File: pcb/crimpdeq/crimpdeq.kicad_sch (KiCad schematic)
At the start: 49 parts, among them J2 USB4105-GF-A, Q1 SS8550, Q2 DMG3415U, SW1 SW_Push, SW2 SW_Push, U1 ESP32-C3-MINI-1, U2 MCP73831T-2ACI/OT, U3 HX711, U4 Rust_Board, U6 SY8088

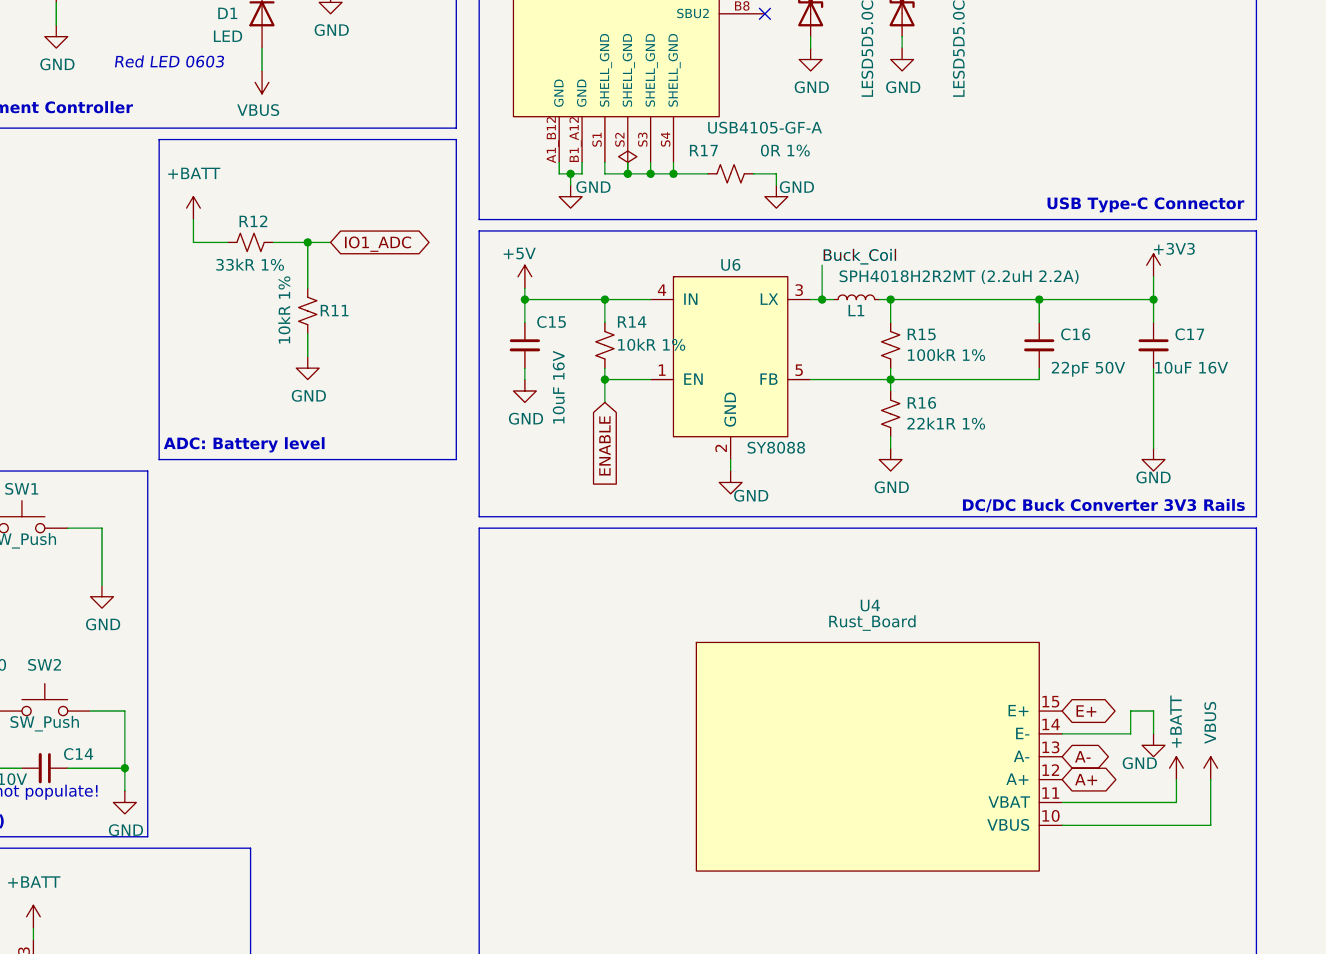
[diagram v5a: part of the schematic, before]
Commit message: fix: allow battery charging while powered off
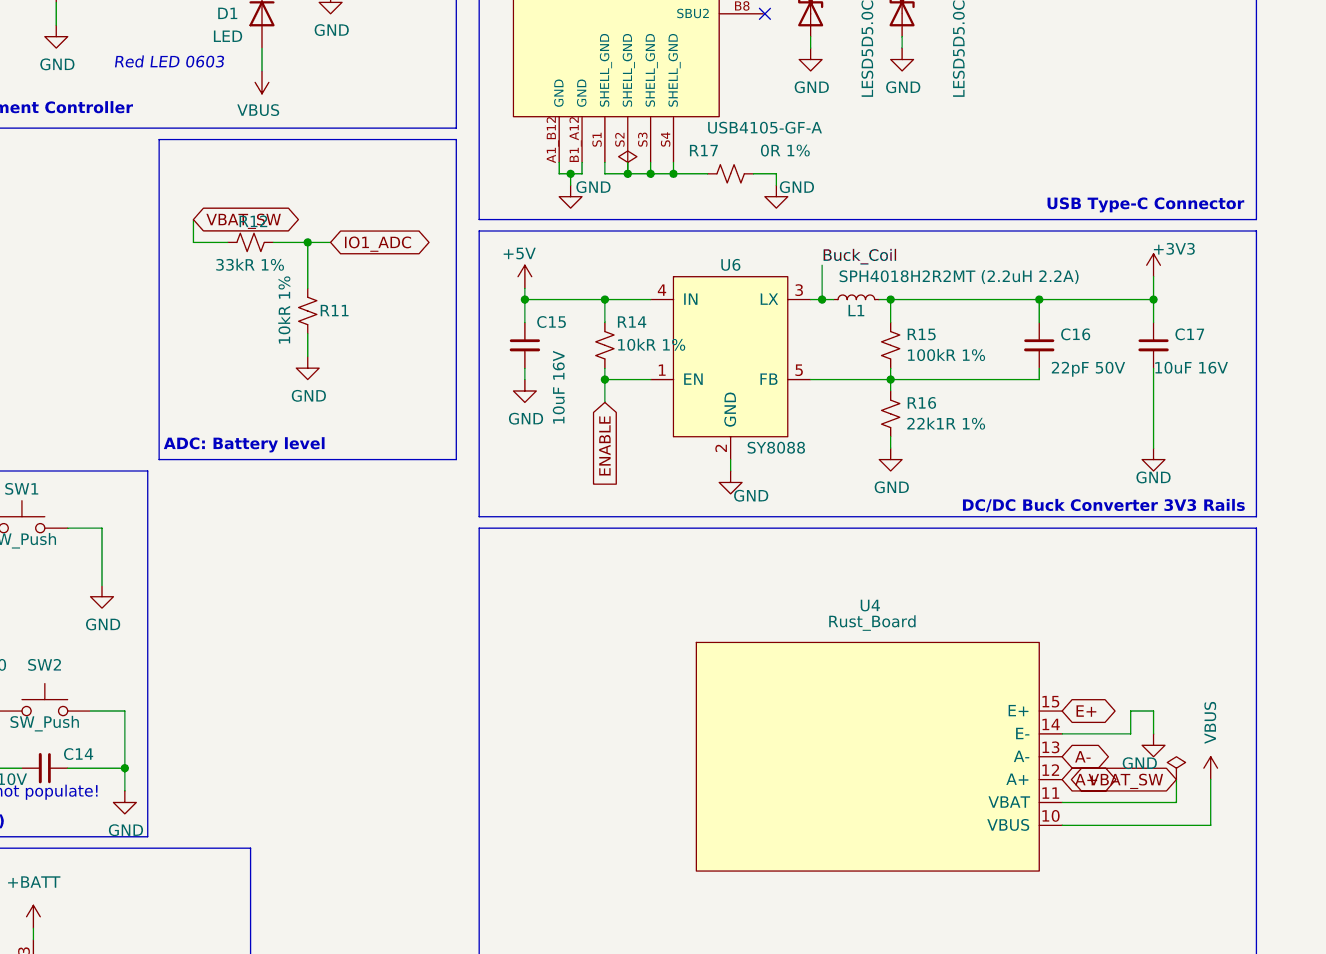
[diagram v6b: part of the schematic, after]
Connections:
- net +BATT: no longer R12.1, U4.11 (VBAT)
- new net VBAT_SW: R12.1, U4.11 (VBAT)
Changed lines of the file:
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@@
 		)
 	)
-	(symbol
-		(lib_id "power:+BATT")
-		(at 275.59 130.81 0)
-		(unit 1)
-		(body_style 1)
-		(exclude_from_sim no)
-		(in_bom yes)
-		(on_board yes)
-		(in_pos_files yes)
-		(dnp no)
-		(property "Reference" "#PWR037"
-			(at 275.59 134.62 0)
-			(hide yes)
-			(show_name no)
-			(do_not_autoplace no)
-			(effects
-				(font
-					(size 1.27 1.27)
-				)
-			)
-		)
-		(property "Value" "+BATT"
-			(at 275.59 124.46 90)
-			(show_name no)
-			(do_not_autoplace no)
-			(effects
-				(font
-					(size 1.27 1.27)
-				)
-			)
-		)
-		(property "Footprint" ""
-			(at 275.59 130.81 0)
-			(hide yes)
-			(show_name no)
-			(do_not_autoplace no)
-			(effects
-				(font
-					(size 1.27 1.27)
-				)
-			)
-		)
-		(property "Datasheet" ""
-			(at 275.59 130.81 0)
-			(hide yes)
-			(show_name no)
-			(do_not_autoplace no)
-			(effects
-				(font
-					(size 1.27 1.27)
-				)
-			)
-		)
-		(property "Description" ""
-			(at 275.59 130.81 0)
-			(hide yes)
-			(show_name no)
-			(do_not_autoplace no)
-			(effects
-				(font
-					(size 1.27 1.27)
-				)
-			)
-		)
-		(pin "1"
-		)
-		(instances
-			(project "crimpdeq"
-				(path "/eb289f4a-30cd-4b15-be5d-5da73d92c8be"
-					(reference "#PWR037")
-					(unit 1)
-				)
+	(global_label "VBAT_SW"
+		(shape bidirectional)
+		(at 275.59 130.81 180)
+		(fields_autoplaced yes)
+		(effects
+			(font
+				(size 1.27 1.27)
+			)
+			(justify right)
+		)
+		(property "Intersheetrefs" "${INTERSHEET_REFS}"
+			(at 264.0433 130.81 0)
+			(effects
+				(font
+					(size 1.27 1.27)
+				)
+				(justify right)
+				(hide yes)
 			)
 		)
@@
 		)
 	)
-	(symbol
-		(lib_id "power:+BATT")
+	(global_label "VBAT_SW"
+		(shape bidirectional)
 		(at 166.37 68.58 0)
-		(unit 1)
-		(body_style 1)
-		(exclude_from_sim no)
-		(in_bom yes)
-		(on_board yes)
-		(in_pos_files yes)
-		(dnp no)
-		(property "Reference" "#PWR031"
-			(at 166.37 72.39 0)
-			(hide yes)
-			(show_name no)
-			(do_not_autoplace no)
-			(effects
-				(font
-					(size 1.27 1.27)
-				)
-			)
-		)
-		(property "Value" "+BATT"
-			(at 166.37 63.5 0)
-			(show_name no)
-			(do_not_autoplace no)
-			(effects
-				(font
-					(size 1.27 1.27)
-				)
-			)
-		)
-		(property "Footprint" ""
-			(at 166.37 68.58 0)
-			(hide yes)
-			(show_name no)
-			(do_not_autoplace no)
-			(effects
-				(font
-					(size 1.27 1.27)
-				)
-			)
-		)
-		(property "Datasheet" ""
-			(at 166.37 68.58 0)
-			(hide yes)
-			(show_name no)
-			(do_not_autoplace no)
-			(effects
-				(font
-					(size 1.27 1.27)
-				)
-			)
-		)
-		(property "Description" ""
-			(at 166.37 68.58 0)
-			(hide yes)
-			(show_name no)
-			(do_not_autoplace no)
-			(effects
-				(font
-					(size 1.27 1.27)
-				)
-			)
-		)
-		(pin "1"
-		)
-		(instances
-			(project "crimpdeq"
-				(path "/eb289f4a-30cd-4b15-be5d-5da73d92c8be"
-					(reference "#PWR031")
-					(unit 1)
-				)
+		(fields_autoplaced yes)
+		(effects
+			(font
+				(size 1.27 1.27)
+			)
+			(justify left)
+		)
+		(property "Intersheetrefs" "${INTERSHEET_REFS}"
+			(at 178.9048 68.58 0)
+			(effects
+				(font
+					(size 1.27 1.27)
+				)
+				(justify left)
+				(hide yes)
 			)
 		)
@@
 	)
 	(embedded_fonts no)
+(symbol
+		(lib_id "power:PWR_FLAG")
+		(at 275.59 130.81 0)
+		(unit 1)
+		(exclude_from_sim no)
+		(in_bom yes)
+		(on_board yes)
+		(dnp no)
+		(property "Reference" "#FLG08"
+			(at 275.59 132.715 0)
+			(effects
+				(font
+					(size 1.27 1.27)
+				)
+				(hide yes)
+			)
+		)
+		(property "Value" "PWR_FLAG"
+			(at 275.59 134.62 0)
+			(effects
+				(font
+					(size 1.27 1.27)
+				)
+				(hide yes)
+			)
+		)
+		(property "Footprint" ""
+			(at 275.59 130.81 0)
+			(effects
+				(font
+					(size 1.27 1.27)
+				)
+				(hide yes)
+			)
+		)
+		(property "Datasheet" "~"
+			(at 275.59 130.81 0)
+			(effects
+				(font
+					(size 1.27 1.27)
+				)
+				(hide yes)
+			)
+		)
+		(property "Description" "Special symbol for telling ERC where power comes from"
+			(at 275.59 130.81 0)
+			(effects
+				(font
+					(size 1.27 1.27)
+				)
+				(hide yes)
+			)
+		)
+		(pin "1"
+		)
+		(instances
+			(project "crimpdeq"
+				(path "/eb289f4a-30cd-4b15-be5d-5da73d92c8be"
+					(reference "#FLG08")
+					(unit 1)
+				)
+			)
+		)
+	)
 )

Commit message: refactor: clarify system power rail naming
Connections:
- net +5V renamed VSYS
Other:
- note added: "USB / Battery VSYS power path"
- note added: "VBUS = USB input +BATT = raw battery VBAT_SW = switched battery VSYS = USB/battery-selected system / buck input"
- note removed: "USB & Battery Switch"
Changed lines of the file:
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@@
 		)
 	)
-	(text "USB & Battery Switch\n"
+	(text "USB / Battery VSYS power path\n"
 		(exclude_from_sim no)
 		(at 161.036 177.546 0)
@@
 		)
 	)
-	(symbol
-		(lib_id "power:+5V")
+	(global_label "VSYS"
+		(shape bidirectional)
 		(at 203.2 76.2 0)
-		(unit 1)
-		(body_style 1)
-		(exclude_from_sim no)
-		(in_bom yes)
-		(on_board yes)
-		(in_pos_files yes)
-		(dnp no)
-		(property "Reference" "#PWR039"
-			(at 203.2 80.01 0)
-			(hide yes)
-			(show_name no)
-			(do_not_autoplace no)
-			(effects
-				(font
-					(size 1.27 1.27)
-				)
+		(fields_autoplaced yes)
+		(effects
+			(font
+				(size 1.27 1.27)
 			)
+			(justify left)
 		)
-		(property "Value" "+5V"
-			(at 200.66 72.39 0)
-			(show_name no)
-			(do_not_autoplace no)
+		(property "Intersheetrefs" "${INTERSHEET_REFS}"
+			(at 209.9575 76.2 0)
 			(effects
 				(font
@@
 				)
 				(justify left)
-			)
-		)
-		(property "Footprint" ""
-			(at 203.2 76.2 0)
-			(hide yes)
-			(show_name no)
-			(do_not_autoplace no)
-			(effects
-				(font
-					(size 1.27 1.27)
-				)
-			)
-		)
-		(property "Datasheet" ""
-			(at 203.2 76.2 0)
-			(hide yes)
-			(show_name no)
-			(do_not_autoplace no)
-			(effects
-				(font
-					(size 1.27 1.27)
-				)
-			)
-		)
-		(property "Description" ""
-			(at 203.2 76.2 0)
-			(hide yes)
-			(show_name no)
-			(do_not_autoplace no)
-			(effects
-				(font
-					(size 1.27 1.27)
-				)
-			)
-		)
-		(pin "1"
-		)
-		(instances
-			(project "crimpdeq"
-				(path "/eb289f4a-30cd-4b15-be5d-5da73d92c8be"
-					(reference "#PWR039")
-					(unit 1)
-				)
+				(hide yes)
 			)
 		)
@@
 		)
 	)
-	(symbol
-		(lib_id "power:+5V")
+	(global_label "VSYS"
+		(shape bidirectional)
 		(at 154.94 160.02 270)
-		(unit 1)
-		(body_style 1)
-		(exclude_from_sim no)
-		(in_bom yes)
-		(on_board yes)
-		(in_pos_files yes)
-		(dnp no)
-		(property "Reference" "#PWR027"
-			(at 151.13 160.02 0)
-			(hide yes)
-			(show_name no)
-			(do_not_autoplace no)
-			(effects
-				(font
-					(size 1.27 1.27)
-				)
-			)
-		)
-		(property "Value" "+5V"
-			(at 157.48 160.02 90)
-			(show_name no)
-			(do_not_autoplace no)
-			(effects
-				(font
-					(size 1.27 1.27)
-				)
-				(justify left)
-			)
-		)
-		(property "Footprint" ""
-			(at 154.94 160.02 0)
-			(hide yes)
-			(show_name no)
-			(do_not_autoplace no)
-			(effects
-				(font
-					(size 1.27 1.27)
-				)
-			)
-		)
-		(property "Datasheet" ""
-			(at 154.94 160.02 0)
-			(hide yes)
-			(show_name no)
-			(do_not_autoplace no)
-			(effects
-				(font
-					(size 1.27 1.27)
-				)
+		(fields_autoplaced yes)
+		(effects
+			(font
+				(size 1.27 1.27)
 			)
+			(justify right)
 		)
-		(property "Description" ""
-			(at 154.94 160.02 0)
-			(hide yes)
-			(show_name no)
-			(do_not_autoplace no)
+		(property "Intersheetrefs" "${INTERSHEET_REFS}"
+			(at 154.94 168.6116 90)
 			(effects
 				(font
 					(size 1.27 1.27)
 				)
-			)
-		)
-		(pin "1"
-		)
-		(instances
-			(project "crimpdeq"
-				(path "/eb289f4a-30cd-4b15-be5d-5da73d92c8be"
-					(reference "#PWR027")
-					(unit 1)
-				)
+				(justify right)
+				(hide yes)
 			)
 		)
@@
 		)
 	)
+(text "VBUS = USB input\n+BATT = raw battery\nVBAT_SW = switched battery\nVSYS = USB/battery-selected system / buck input"
+		(exclude_from_sim no)
+		(at 160.782 180.594 0)
+		(effects
+			(font
+				(size 1.27 1.27)
+			)
+			(justify left top)
+		)
+	)

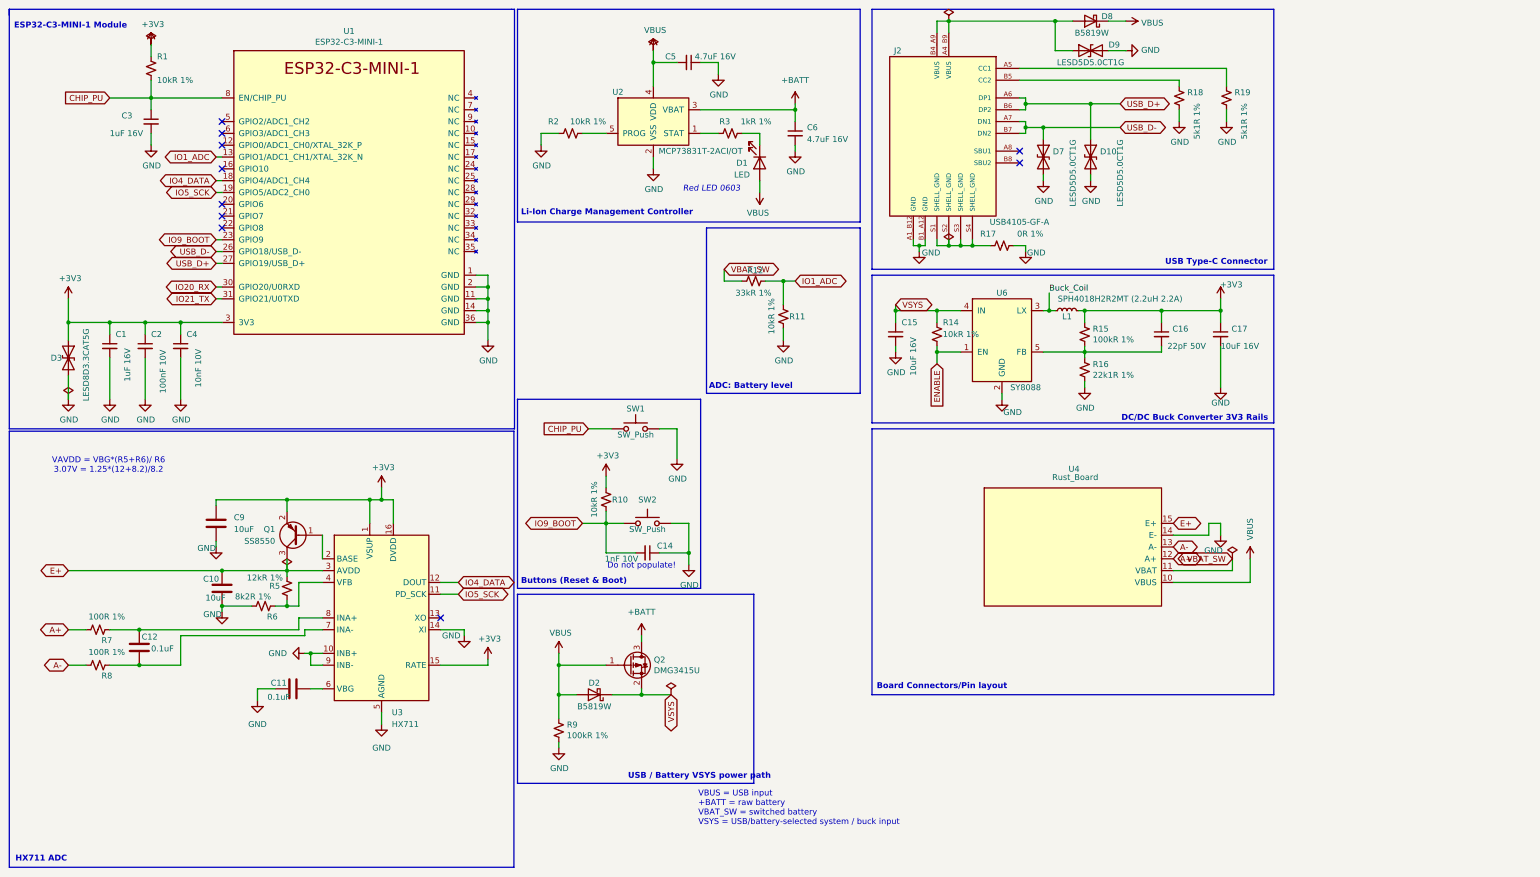
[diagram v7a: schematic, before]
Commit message: feat: Add rbg led and route it
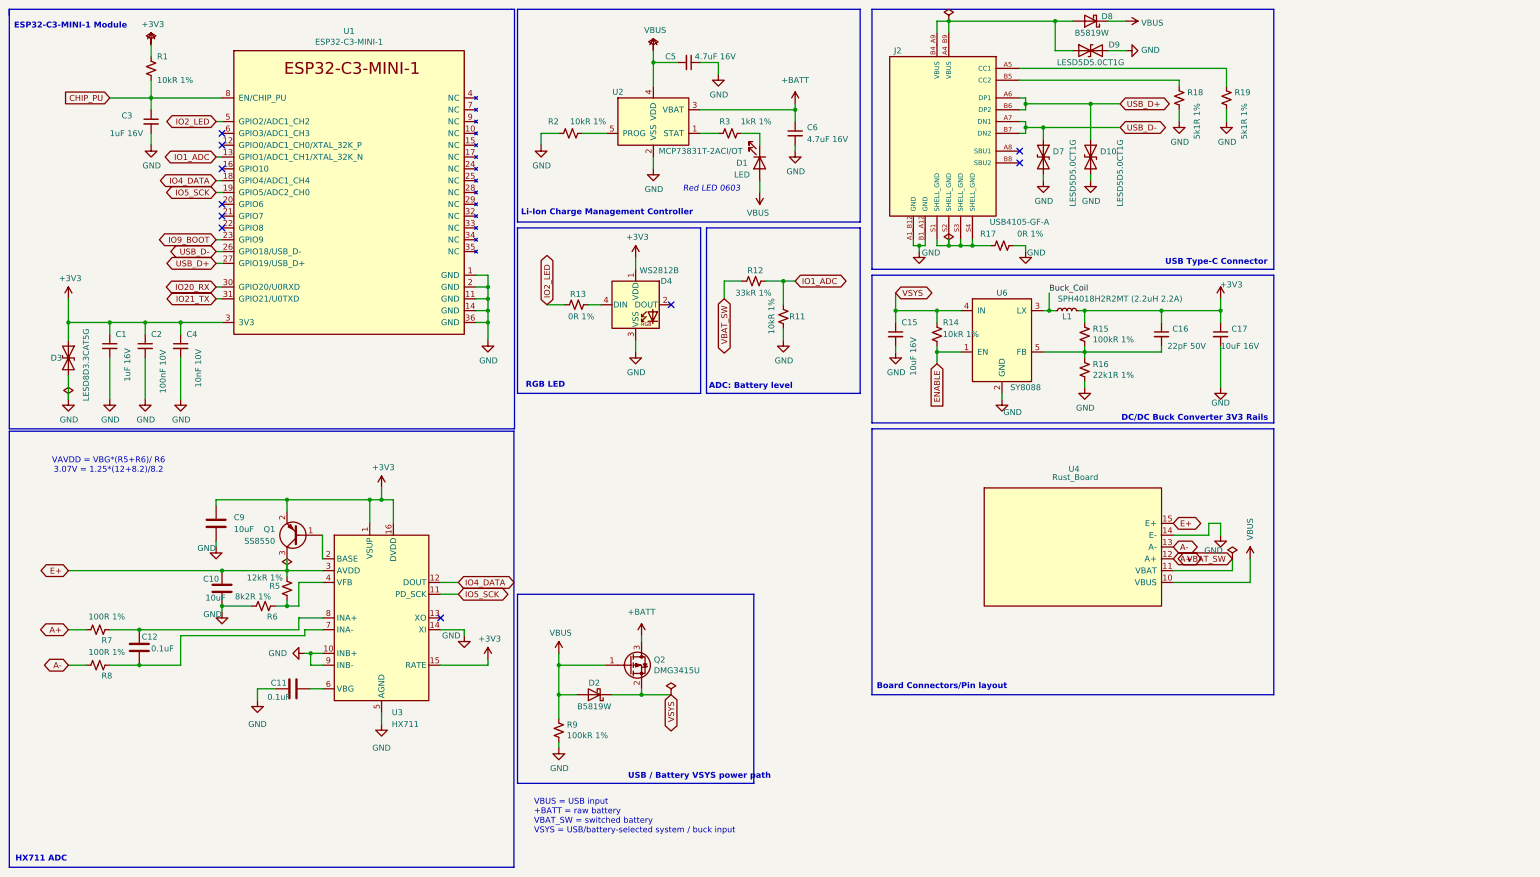
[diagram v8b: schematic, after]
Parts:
- removed C14: 1nF 10V, Capacitor_SMD:C_0402_1005Metric, symbol Device:C_Small
- removed R10: 10kR 1%, Resistor_SMD:R_0402_1005Metric, symbol Device:R_Small_US
- removed SW1, SW2: SW_Push, Button_Switch_SMD:SW_SPST_PTS810, symbol Switch:SW_Push
- added D4: WS2812B, LED_SMD:LED_WS2812B_PLCC4_5.0x5.0mm_P3.2mm, symbol LED:WS2812B
- added R13: 0R 1%, Resistor_SMD:R_0402_1005Metric, symbol Device:R_Small_US
- U4: footprint Rust_Board:Rust_Board -> (none)
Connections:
- net +3V3: now also D4.1 (VDD)
- net GND: now also D4.3 (VSS)
- net IO2_LED: now reaches U1.5 (GPIO2/ADC1_CH2)
- net IO2_LED: now also R13.1
- new net: D4.4 (DIN), R13.2
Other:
- note added: "RGB LED"
- note removed: "Buttons (Reset & Boot)"
- note removed: "Do not populate!"
